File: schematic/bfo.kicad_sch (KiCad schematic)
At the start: 34 parts, among them Q10 2N7000, Q6 2N3904, Q7 2N3904, Y1 9.000, Y2 9.000, Y3 9.000

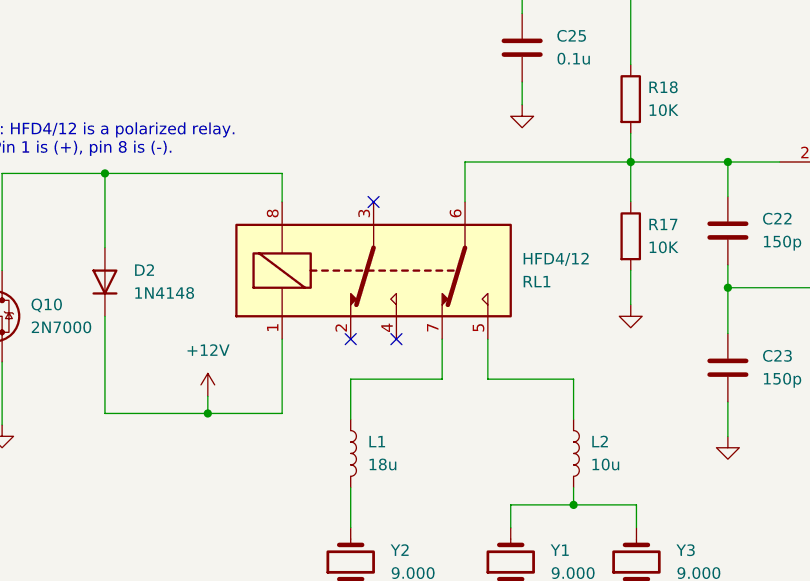
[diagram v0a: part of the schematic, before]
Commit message: Schematic: minor changes
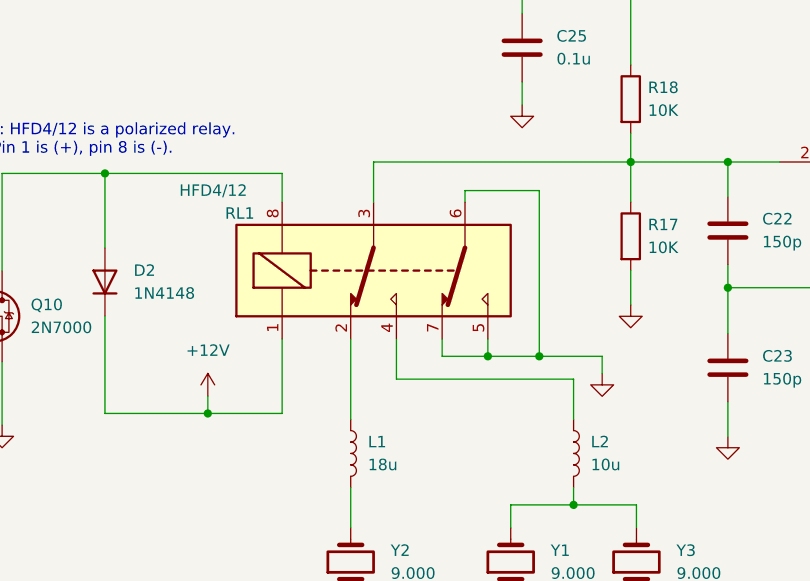
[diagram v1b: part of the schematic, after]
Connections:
- net GND: now also RL1.5, RL1.6, RL1.7
- net at C22.1, Q6.2 (B), R17.1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: now also RL1.3; no longer RL1.6
- net at RL1.2: now also L1.1
- net at RL1.4: now also L2.1
- no-connect marks 6 -> 3
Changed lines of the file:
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@@
   (junction (at 63.5 85.09) (diameter 0) (color 0 0 0 0)
   )
+  (junction (at 106.045 105.41) (diameter 0) (color 0 0 0 0)
+  )
   (junction (at 233.045 109.22) (diameter 0) (color 0 0 0 0)
   )
   (junction (at 247.015 99.06) (diameter 0) (color 0 0 0 0)
   )
+  (junction (at 111.76 105.41) (diameter 0) (color 0 0 0 0)
+  )
   (junction (at 109.855 63.5) (diameter 0) (color 0 0 0 0)
   )
@@
   (junction (at 218.44 109.22) (diameter 0) (color 0 0 0 0)
   )
-  (no_connect (at 95.885 103.505))
   (no_connect (at 264.16 116.84))
-  (no_connect (at 93.345 88.265))
   (no_connect (at 264.16 121.92))
-  (no_connect (at 90.805 103.505))
   (no_connect (at 248.92 119.38))
   (wire (pts (xy 121.92 63.5) (xy 121.92 73.025))
@@
     (stroke (width 0) (type default))
   )
-  (wire (pts (xy 106.045 103.505) (xy 106.045 107.95))
-    (stroke (width 0) (type default))
-  )
   (wire (pts (xy 187.325 109.22) (xy 191.135 109.22))
     (stroke (width 0) (type default))
@@
     (stroke (width 0) (type default))
   )
-  (wire (pts (xy 103.505 83.82) (xy 121.92 83.82))
+  (wire (pts (xy 93.345 83.82) (xy 121.92 83.82))
+    (stroke (width 0) (type default))
+  )
+  (wire (pts (xy 100.965 105.41) (xy 100.965 103.505))
+    (stroke (width 0) (type default))
+  )
+  (wire (pts (xy 118.745 105.41) (xy 111.76 105.41))
     (stroke (width 0) (type default))
   )
@@
     (stroke (width 0) (type default))
   )
+  (wire (pts (xy 118.745 107.315) (xy 118.745 105.41))
+    (stroke (width 0) (type default))
+  )
   (wire (pts (xy 228.6 109.22) (xy 233.045 109.22))
     (stroke (width 0) (type default))
@@
     (stroke (width 0) (type default))
   )
+  (wire (pts (xy 106.045 105.41) (xy 100.965 105.41))
+    (stroke (width 0) (type default))
+  )
   (wire (pts (xy 109.855 63.5) (xy 109.855 67.31))
     (stroke (width 0) (type default))
@@
     (stroke (width 0) (type default))
   )
+  (wire (pts (xy 103.505 88.265) (xy 103.505 86.995))
+    (stroke (width 0) (type default))
+  )
   (wire (pts (xy 115.57 144.78) (xy 115.57 147.955))
     (stroke (width 0) (type default))
@@
     (stroke (width 0) (type default))
   )
-  (wire (pts (xy 100.965 107.95) (xy 100.965 103.505))
-    (stroke (width 0) (type default))
-  )
   (wire (pts (xy 205.74 121.285) (xy 205.74 123.825))
     (stroke (width 0) (type default))
@@
     (stroke (width 0) (type default))
   )
-  (wire (pts (xy 103.505 88.265) (xy 103.505 83.82))
-    (stroke (width 0) (type default))
-  )
   (wire (pts (xy 74.93 111.76) (xy 83.185 111.76))
     (stroke (width 0) (type default))
@@
     (stroke (width 0) (type default))
   )
+  (wire (pts (xy 111.76 86.995) (xy 111.76 105.41))
+    (stroke (width 0) (type default))
+  )
   (wire (pts (xy 266.065 84.455) (xy 266.065 80.01))
     (stroke (width 0) (type default))
@@
     (stroke (width 0) (type default))
   )
-  (wire (pts (xy 90.805 112.395) (xy 90.805 107.95))
-    (stroke (width 0) (type default))
-  )
   (wire (pts (xy 115.57 107.95) (xy 115.57 112.395))
     (stroke (width 0) (type default))
@@
     (stroke (width 0) (type default))
   )
+  (wire (pts (xy 111.76 105.41) (xy 106.045 105.41))
+    (stroke (width 0) (type default))
+  )
   (wire (pts (xy 121.92 95.885) (xy 121.92 99.695))
     (stroke (width 0) (type default))
@@
     (stroke (width 0) (type default))
   )
+  (wire (pts (xy 103.505 86.995) (xy 111.76 86.995))
+    (stroke (width 0) (type default))
+  )
   (wire (pts (xy 63.5 100.965) (xy 63.5 111.76))
     (stroke (width 0) (type default))
   )
-  (wire (pts (xy 90.805 107.95) (xy 100.965 107.95))
-    (stroke (width 0) (type default))
-  )
   (wire (pts (xy 52.07 85.09) (xy 52.07 95.885))
     (stroke (width 0) (type default))
   )
+  (wire (pts (xy 95.885 103.505) (xy 95.885 107.95))
+    (stroke (width 0) (type default))
+  )
   (wire (pts (xy 63.5 85.09) (xy 83.185 85.09))
     (stroke (width 0) (type default))
@@
     (stroke (width 0) (type default))
   )
+  (wire (pts (xy 90.805 103.505) (xy 90.805 112.395))
+    (stroke (width 0) (type default))
+  )
   (wire (pts (xy 170.815 118.745) (xy 170.815 123.825))
     (stroke (width 0) (type default))
   )
+  (wire (pts (xy 93.345 88.265) (xy 93.345 83.82))
+    (stroke (width 0) (type default))
+  )
   (wire (pts (xy 122.555 121.92) (xy 122.555 124.46))
     (stroke (width 0) (type default))
@@
     (stroke (width 0) (type default))
   )
-  (wire (pts (xy 106.045 107.95) (xy 115.57 107.95))
+  (wire (pts (xy 95.885 107.95) (xy 115.57 107.95))
     (stroke (width 0) (type default))
   )
@@
   )
   (wire (pts (xy 83.185 111.76) (xy 83.185 103.505))
+    (stroke (width 0) (type default))
+  )
+  (wire (pts (xy 106.045 103.505) (xy 106.045 105.41))
     (stroke (width 0) (type default))
   )
@@
   (symbol (lib_id "Relay:G2RL-2-ASI-DC5") (at 93.345 95.885 0) (mirror x) (unit 1)
     (in_bom yes) (on_board yes) (dnp no)
-    (property "Reference" "RL1" (at 109.855 97.155 0)
-      (effects (font (size 1.27 1.27)) (justify left))
-    )
-    (property "Value" "HFD4/12" (at 109.855 94.615 0)
+    (property "Reference" "RL1" (at 76.835 89.535 0)
+      (effects (font (size 1.27 1.27)) (justify left))
+    )
+    (property "Value" "HFD4/12" (at 71.755 86.995 0)
       (effects (font (size 1.27 1.27)) (justify left))
     )
@@
         )
       )
+    )
+  )
+  (symbol (lib_id "power:GND") (at 118.745 107.315 0) (unit 1)
+    (in_bom yes) (on_board yes) (dnp no) (fields_autoplaced)
+    (property "Reference" "#PWR0257" (at 118.745 113.665 0)
+      (effects (font (size 1.27 1.27)) hide)
+    )
+    (property "Value" "GND" (at 118.745 111.76 0)
+      (effects (font (size 1.27 1.27)) hide)
+    )
+    (property "Footprint" "" (at 118.745 107.315 0)
+      (effects (font (size 1.27 1.27)) hide)
+    )
+    (property "Datasheet" "" (at 118.745 107.315 0)
+      (effects (font (size 1.27 1.27)) hide)
+    )
+    (pin "1")
+    (instances
+      (project "hbr-mk2"
+        (path "/700c9878-4ed7-49d5-a273-77cf9d92989d/f830f485-dae1-49b8-8b15-2f9b2d30db58"
+          (reference "#PWR0257") (unit 1)
+        )
+      )

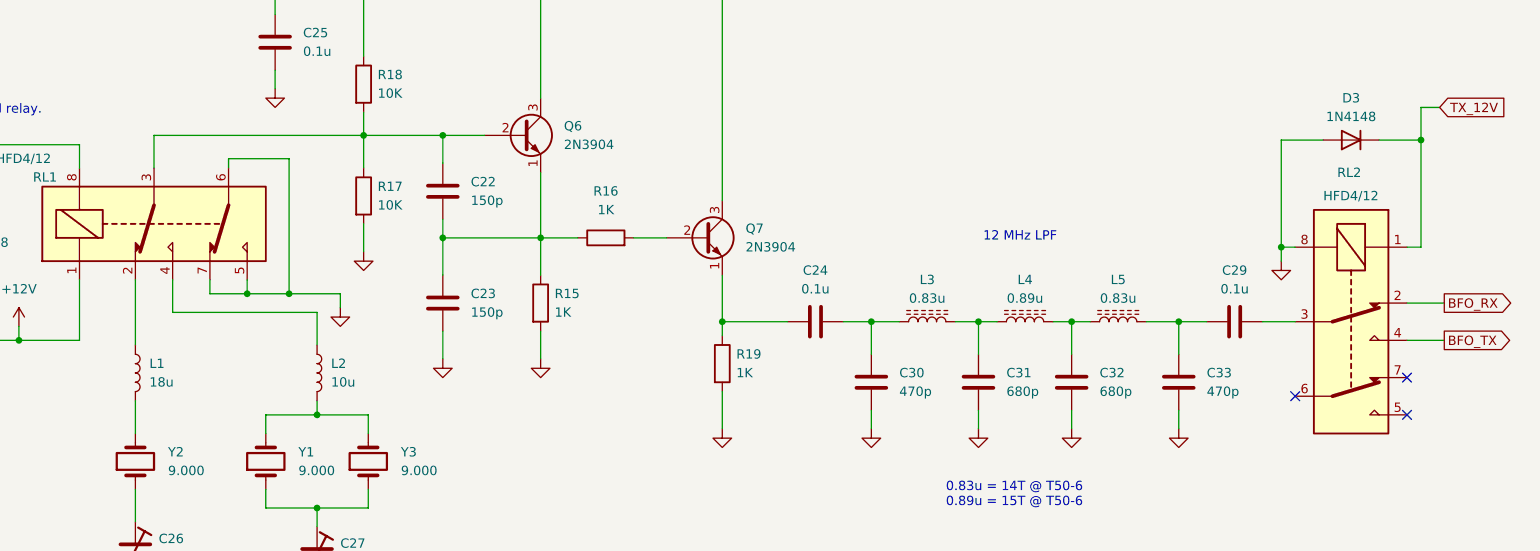
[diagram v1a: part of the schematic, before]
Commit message: Connect relay contact groups in parallel where appropriate
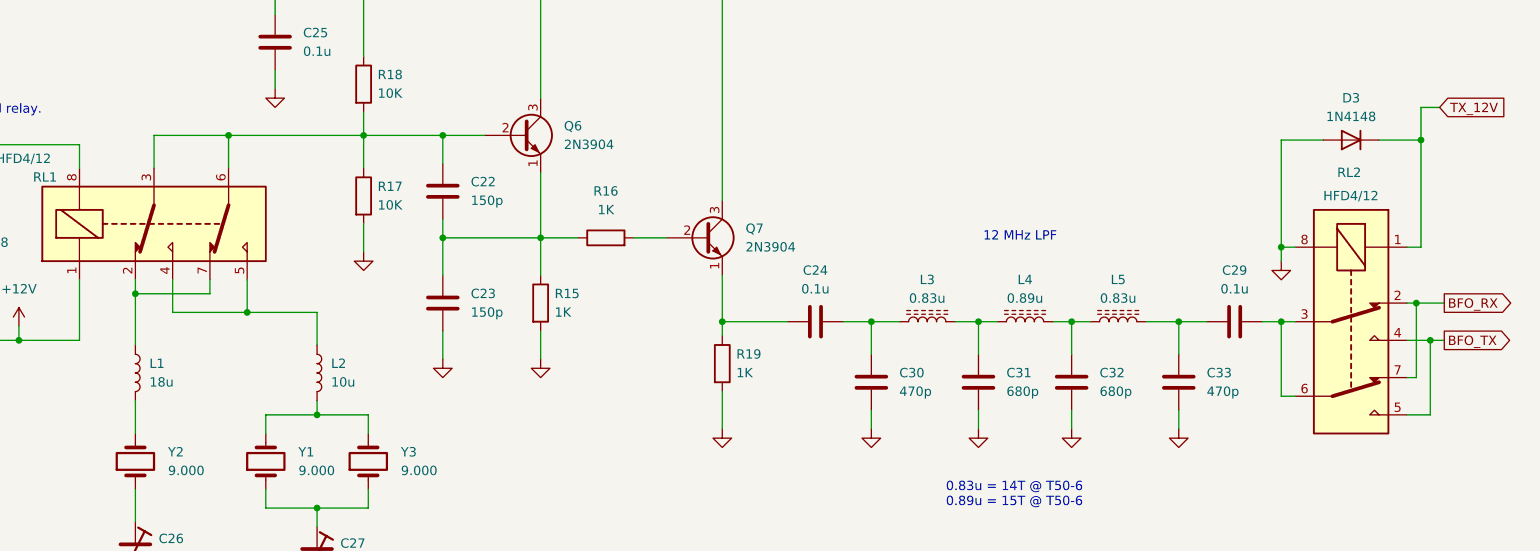
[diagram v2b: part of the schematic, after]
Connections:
- net BFO_RX: now also RL2.7
- net BFO_TX: now also RL2.5
- net GND: no longer RL1.5, RL1.6, RL1.7
- net at C22.1, Q6.2 (B), R17.1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: now also RL1.6
- net at L1.1, RL1.2: now also RL1.7
- net at L2.1, RL1.4: now also RL1.5
- net at C29.2, RL2.3: now also RL2.6
- no-connect marks 3 -> 0
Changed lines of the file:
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@@
 (kicad_sch (version 20230121) (generator eeschema)
   (paper "A4")
+  (junction (at 265.43 106.68) (diameter 0) (color 0 0 0 0)
+  )
+  (junction (at 106.045 107.95) (diameter 0) (color 0 0 0 0)
+  )
   (junction (at 132.715 97.79) (diameter 0) (color 0 0 0 0)
   )
@@
   (junction (at 170.815 109.22) (diameter 0) (color 0 0 0 0)
   )
+  (junction (at 247.015 109.22) (diameter 0) (color 0 0 0 0)
+  )
   (junction (at 63.5 85.09) (diameter 0) (color 0 0 0 0)
   )
-  (junction (at 106.045 105.41) (diameter 0) (color 0 0 0 0)
+  (junction (at 103.505 83.82) (diameter 0) (color 0 0 0 0)
   )
   (junction (at 233.045 109.22) (diameter 0) (color 0 0 0 0)
   )
+  (junction (at 90.805 105.41) (diameter 0) (color 0 0 0 0)
+  )
   (junction (at 247.015 99.06) (diameter 0) (color 0 0 0 0)
   )
-  (junction (at 111.76 105.41) (diameter 0) (color 0 0 0 0)
-  )
   (junction (at 109.855 63.5) (diameter 0) (color 0 0 0 0)
   )
@@
   (junction (at 218.44 109.22) (diameter 0) (color 0 0 0 0)
   )
-  (no_connect (at 264.16 116.84))
-  (no_connect (at 264.16 121.92))
-  (no_connect (at 248.92 119.38))
+  (junction (at 267.335 111.76) (diameter 0) (color 0 0 0 0)
+  )
   (wire (pts (xy 121.92 63.5) (xy 121.92 73.025))
     (stroke (width 0) (type default))
@@
     (stroke (width 0) (type default))
   )
-  (wire (pts (xy 93.345 83.82) (xy 121.92 83.82))
+  (wire (pts (xy 93.345 83.82) (xy 103.505 83.82))
     (stroke (width 0) (type default))
   )
@@
     (stroke (width 0) (type default))
   )
-  (wire (pts (xy 118.745 105.41) (xy 111.76 105.41))
-    (stroke (width 0) (type default))
-  )
   (wire (pts (xy 191.135 121.285) (xy 191.135 123.825))
     (stroke (width 0) (type default))
   )
-  (wire (pts (xy 118.745 107.315) (xy 118.745 105.41))
-    (stroke (width 0) (type default))
-  )
   (wire (pts (xy 228.6 109.22) (xy 233.045 109.22))
     (stroke (width 0) (type default))
@@
     (stroke (width 0) (type default))
   )
-  (wire (pts (xy 106.045 105.41) (xy 100.965 105.41))
-    (stroke (width 0) (type default))
-  )
   (wire (pts (xy 109.855 63.5) (xy 109.855 67.31))
     (stroke (width 0) (type default))
@@
     (stroke (width 0) (type default))
   )
-  (wire (pts (xy 103.505 88.265) (xy 103.505 86.995))
+  (wire (pts (xy 103.505 83.82) (xy 103.505 88.265))
     (stroke (width 0) (type default))
   )
@@
     (stroke (width 0) (type default))
   )
-  (wire (pts (xy 264.16 106.68) (xy 269.24 106.68))
+  (wire (pts (xy 264.16 106.68) (xy 265.43 106.68))
     (stroke (width 0) (type default))
   )
@@
     (stroke (width 0) (type default))
   )
+  (wire (pts (xy 247.015 109.22) (xy 248.92 109.22))
+    (stroke (width 0) (type default))
+  )
   (wire (pts (xy 218.44 109.22) (xy 220.98 109.22))
     (stroke (width 0) (type default))
@@
     (stroke (width 0) (type default))
   )
+  (wire (pts (xy 90.805 105.41) (xy 100.965 105.41))
+    (stroke (width 0) (type default))
+  )
   (wire (pts (xy 52.07 85.09) (xy 63.5 85.09))
     (stroke (width 0) (type default))
@@
     (stroke (width 0) (type default))
   )
+  (wire (pts (xy 267.335 121.92) (xy 267.335 111.76))
+    (stroke (width 0) (type default))
+  )
+  (wire (pts (xy 267.335 111.76) (xy 269.24 111.76))
+    (stroke (width 0) (type default))
+  )
   (wire (pts (xy 121.92 63.5) (xy 146.05 63.5))
     (stroke (width 0) (type default))
@@
     (stroke (width 0) (type default))
   )
+  (wire (pts (xy 264.16 121.92) (xy 267.335 121.92))
+    (stroke (width 0) (type default))
+  )
   (wire (pts (xy 109.855 59.055) (xy 109.855 63.5))
     (stroke (width 0) (type default))
@@
     (stroke (width 0) (type default))
   )
+  (wire (pts (xy 248.92 119.38) (xy 247.015 119.38))
+    (stroke (width 0) (type default))
+  )
   (wire (pts (xy 109.855 63.5) (xy 121.92 63.5))
     (stroke (width 0) (type default))
   )
+  (wire (pts (xy 265.43 106.68) (xy 269.24 106.68))
+    (stroke (width 0) (type default))
+  )
   (wire (pts (xy 146.05 97.79) (xy 151.13 97.79))
     (stroke (width 0) (type default))
@@
     (stroke (width 0) (type default))
   )
-  (wire (pts (xy 111.76 86.995) (xy 111.76 105.41))
-    (stroke (width 0) (type default))
-  )
   (wire (pts (xy 266.065 84.455) (xy 266.065 80.01))
     (stroke (width 0) (type default))
@@
     (stroke (width 0) (type default))
   )
-  (wire (pts (xy 244.475 109.22) (xy 248.92 109.22))
+  (wire (pts (xy 244.475 109.22) (xy 247.015 109.22))
     (stroke (width 0) (type default))
   )
@@
     (stroke (width 0) (type default))
   )
-  (wire (pts (xy 111.76 105.41) (xy 106.045 105.41))
-    (stroke (width 0) (type default))
-  )
   (wire (pts (xy 121.92 95.885) (xy 121.92 99.695))
     (stroke (width 0) (type default))
@@
     (stroke (width 0) (type default))
   )
+  (wire (pts (xy 90.805 105.41) (xy 90.805 112.395))
+    (stroke (width 0) (type default))
+  )
   (wire (pts (xy 90.805 132.08) (xy 90.805 136.525))
     (stroke (width 0) (type default))
@@
     (stroke (width 0) (type default))
   )
-  (wire (pts (xy 103.505 86.995) (xy 111.76 86.995))
-    (stroke (width 0) (type default))
-  )
   (wire (pts (xy 63.5 100.965) (xy 63.5 111.76))
     (stroke (width 0) (type default))
@@
     (stroke (width 0) (type default))
   )
+  (wire (pts (xy 247.015 119.38) (xy 247.015 109.22))
+    (stroke (width 0) (type default))
+  )
   (wire (pts (xy 95.885 103.505) (xy 95.885 107.95))
     (stroke (width 0) (type default))
@@
     (stroke (width 0) (type default))
   )
-  (wire (pts (xy 90.805 103.505) (xy 90.805 112.395))
+  (wire (pts (xy 90.805 103.505) (xy 90.805 105.41))
     (stroke (width 0) (type default))
   )
@@
     (stroke (width 0) (type default))
   )
+  (wire (pts (xy 265.43 116.84) (xy 265.43 106.68))
+    (stroke (width 0) (type default))
+  )
+  (wire (pts (xy 264.16 116.84) (xy 265.43 116.84))
+    (stroke (width 0) (type default))
+  )
   (wire (pts (xy 191.135 109.22) (xy 194.945 109.22))
     (stroke (width 0) (type default))
@@
     (stroke (width 0) (type default))
   )
-  (wire (pts (xy 95.885 107.95) (xy 115.57 107.95))
+  (wire (pts (xy 95.885 107.95) (xy 106.045 107.95))
     (stroke (width 0) (type default))
   )
@@
     (stroke (width 0) (type default))
   )
+  (wire (pts (xy 106.045 107.95) (xy 115.57 107.95))
+    (stroke (width 0) (type default))
+  )
   (wire (pts (xy 146.05 97.79) (xy 146.05 102.87))
     (stroke (width 0) (type default))
@@
     (stroke (width 0) (type default))
   )
+  (wire (pts (xy 103.505 83.82) (xy 121.92 83.82))
+    (stroke (width 0) (type default))
+  )
   (wire (pts (xy 90.805 124.46) (xy 90.805 120.015))
     (stroke (width 0) (type default))
   )
-  (wire (pts (xy 264.16 111.76) (xy 269.24 111.76))
+  (wire (pts (xy 264.16 111.76) (xy 267.335 111.76))
     (stroke (width 0) (type default))
   )
@@
     (stroke (width 0) (type default))
   )
-  (wire (pts (xy 106.045 103.505) (xy 106.045 105.41))
+  (wire (pts (xy 106.045 103.505) (xy 106.045 107.95))
     (stroke (width 0) (type default))
   )
@@
         )
       )
-    )
-  )
-  (symbol (lib_id "power:GND") (at 118.745 107.315 0) (unit 1)
-    (in_bom yes) (on_board yes) (dnp no) (fields_autoplaced)
-    (property "Reference" "#PWR0257" (at 118.745 113.665 0)
-      (effects (font (size 1.27 1.27)) hide)
-    )
-    (property "Value" "GND" (at 118.745 111.76 0)
-      (effects (font (size 1.27 1.27)) hide)
-    )
-    (property "Footprint" "" (at 118.745 107.315 0)
-      (effects (font (size 1.27 1.27)) hide)
-    )
-    (property "Datasheet" "" (at 118.745 107.315 0)
-      (effects (font (size 1.27 1.27)) hide)
-    )
-    (pin "1")
-    (instances
-      (project "hbr-mk2"
-        (path "/700c9878-4ed7-49d5-a273-77cf9d92989d/f830f485-dae1-49b8-8b15-2f9b2d30db58"
-          (reference "#PWR0257") (unit 1)
-        )
-      )

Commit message: Schematic: minor fixes
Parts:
- L3, L5: value 0.83u -> T50-6
- L4: value 0.89u -> T50-6
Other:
- note added: "0.83u"
- note added: "0.89u"
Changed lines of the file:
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@@
+    (effects (font (size 1.27 1.27)) (justify left bottom))
+  )
+  (text "0.83u" (at 222.25 106.68 0)
+    (effects (font (size 1.27 1.27)) (justify left bottom))
+  )
+  (text "0.83u" (at 196.215 106.68 0)
+    (effects (font (size 1.27 1.27)) (justify left bottom))
+  )
+  (text "0.89u" (at 209.55 106.68 0)
     (effects (font (size 1.27 1.27)) (justify left bottom))
   )
@@
       (effects (font (size 1.27 1.27)))
     )
-    (property "Value" "0.83u" (at 198.755 106.045 90)
-      (effects (font (size 1.27 1.27)))
+    (property "Value" "T50-6" (at 198.755 106.045 90)
+      (effects (font (size 1.27 1.27)) hide)
     )
     (property "Footprint" "" (at 198.755 109.22 0)
@@
       (effects (font (size 1.27 1.27)))
     )
-    (property "Value" "0.83u" (at 224.79 106.045 90)
-      (effects (font (size 1.27 1.27)))
+    (property "Value" "T50-6" (at 224.79 106.045 90)
+      (effects (font (size 1.27 1.27)) hide)
     )
     (property "Footprint" "" (at 224.79 109.22 0)
@@
       (effects (font (size 1.27 1.27)))
     )
-    (property "Value" "0.89u" (at 212.09 106.045 90)
-      (effects (font (size 1.27 1.27)))
+    (property "Value" "T50-6" (at 212.09 106.045 90)
+      (effects (font (size 1.27 1.27)) hide)
     )
     (property "Footprint" "" (at 212.09 109.22 0)
